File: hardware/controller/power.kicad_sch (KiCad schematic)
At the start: 16 parts, among them J11 Barrel_Jack, J7 Conn_01x04_Pin, J8 Conn_01x04_Pin, U7 MPM3606AGQV-P, U8 LM73100RPWR, U9 LM73100RPWR

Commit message: Update component position offsets for JLC
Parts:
- U7: FT Position Offset (none) -> 0,0.6032
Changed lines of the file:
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@@
+			)
+		)
+		(property "FT Position Offset" "0,0.6032"
+			(at 78.74 113.03 0)
+			(effects
+				(font
+					(size 1.27 1.27)
+				)
+				(hide yes)
 			)
 		)

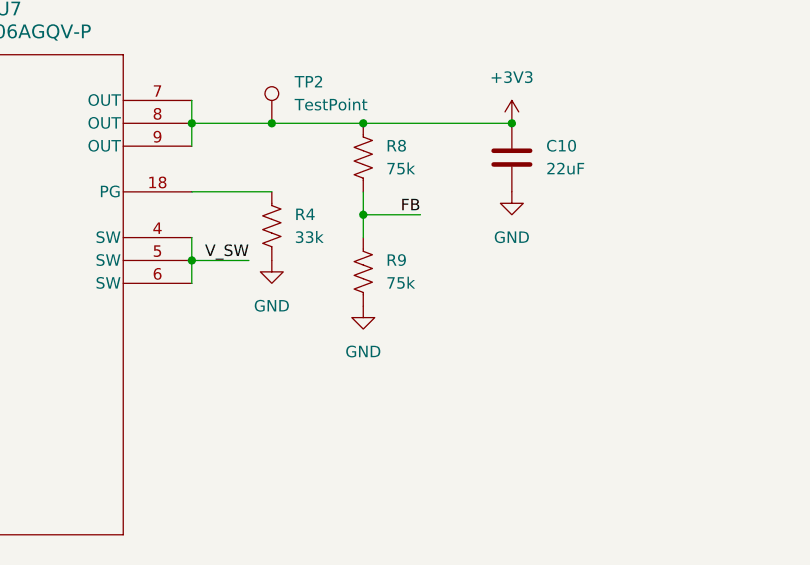
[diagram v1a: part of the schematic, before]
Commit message: Fix resistor on regulator, space out fan headers more
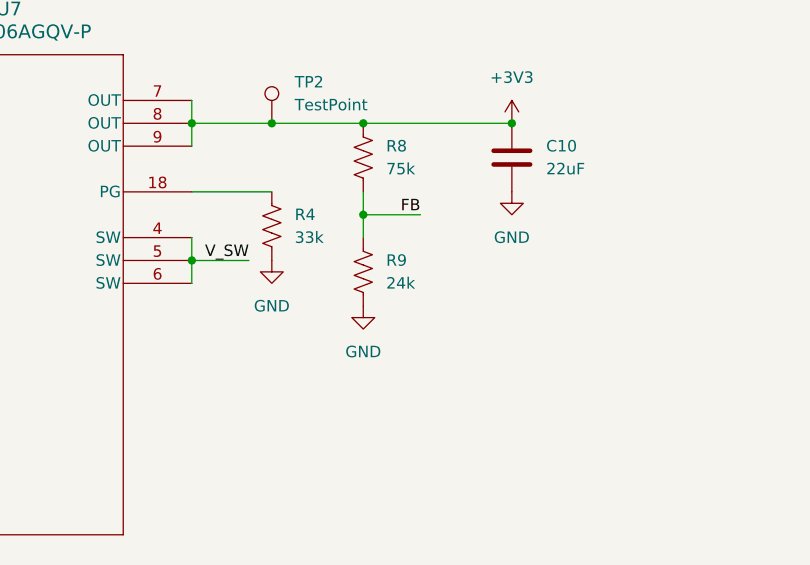
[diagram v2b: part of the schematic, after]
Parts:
- R9: value 75k -> 24k; LCSC C17819 -> C17575
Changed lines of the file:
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@@
 			)
 		)
-		(property "Value" "75k"
+		(property "Value" "24k"
 			(at 140.97 133.3499 0)
 			(effects
@@
 			)
 		)
-		(property "LCSC" "C17819"
+		(property "LCSC" "C17575"
 			(at 138.43 132.08 0)
 			(effects
